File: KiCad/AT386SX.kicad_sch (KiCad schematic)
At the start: 33 parts, among them J10 OSC_PIN1, J11 OSC_PIN8, Q3 2N3904, U2 74HC05, U6 ICW42C07, U7 Cx486SLC, U8 80387SX, U9 RC2016A5, X2 14.31818MHz

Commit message: Version 1.5: Add filtering capacitors
Signed-off-by: Sergey Kiselev <skiselev@gmail.com>
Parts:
- R13: footprint My_Components:Res_Axial_L6.3mm_D2.5mm_P10.16mm_Horizontal -> My_Components:Res_762
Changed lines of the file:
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@@
       (effects (font (size 1.27 1.27)) (justify left))
     )
-    (property "Footprint" "My_Components:Res_Axial_L6.3mm_D2.5mm_P10.16mm_Horizontal" (id 2) (at 239.522 207.01 90)
+    (property "Footprint" "My_Components:Res_762" (id 2) (at 239.522 207.01 90)
       (effects (font (size 1.27 1.27)) hide)
     )
@@
   )
   (symbol_instances
+    (path "/b540f997-cabb-4061-85a0-370b4e9dd03a/c0e940d1-2426-4cbd-9a9b-134c5c650fe6"
+      (reference "#FLG01") (unit 1) (value "PWR_FLAG") (footprint "")
+    )
+    (path "/b540f997-cabb-4061-85a0-370b4e9dd03a/2758a6ac-f07f-4e7c-83ad-7d9a34e4f2bd"
+      (reference "#FLG02") (unit 1) (value "PWR_FLAG") (footprint "")
+    )
     (path "/1c0f074e-275c-4c09-93e3-0959df27fb02/9751a7f0-e700-4753-8324-be24a75a4a6c"
       (reference "#FLG0101") (unit 1) (value "PWR_FLAG") (footprint "")
@@
       (reference "#FLG0103") (unit 1) (value "PWR_FLAG") (footprint "")
     )
-    (path "/b540f997-cabb-4061-85a0-370b4e9dd03a/0338c4db-c33f-45e8-8989-5af966eadf04"
-      (reference "#FLG0104") (unit 1) (value "PWR_FLAG") (footprint "")
-    )
     (path "/b540f997-cabb-4061-85a0-370b4e9dd03a/e285e334-2dc0-407d-a384-e1491c80ffa6"
       (reference "#FLG0105") (unit 1) (value "PWR_FLAG") (footprint "")
     )
-    (path "/b540f997-cabb-4061-85a0-370b4e9dd03a/cdc8d8e2-b0ee-4c76-a0c0-bd7107912b4a"
-      (reference "#FLG0106") (unit 1) (value "PWR_FLAG") (footprint "")
-    )
     (path "/b540f997-cabb-4061-85a0-370b4e9dd03a/1a7d0fff-6458-426d-8397-de30782b2d34"
       (reference "#PWR0101") (unit 1) (value "GND") (footprint "")
@@
       (reference "#PWR0155") (unit 1) (value "VCC") (footprint "")
     )
+    (path "/b540f997-cabb-4061-85a0-370b4e9dd03a/53d85d0a-ae75-44bf-aff8-0d14c3b835b5"
+      (reference "#PWR0156") (unit 1) (value "VCC") (footprint "")
+    )
     (path "/b540f997-cabb-4061-85a0-370b4e9dd03a/f7b625b8-3877-4549-89fa-b234d7c48294"
       (reference "#PWR0157") (unit 1) (value "GND") (footprint "")
     )
-    (path "/b540f997-cabb-4061-85a0-370b4e9dd03a/846cd0cf-749b-4032-9d8a-86cf301d5632"
-      (reference "#PWR0158") (unit 1) (value "VCC") (footprint "")
-    )
     (path "/5f5198df-7309-40ea-b4e0-3ab5dbf9b838"
       (reference "#PWR0159") (unit 1) (value "GND") (footprint "")
@@
       (reference "#PWR0160") (unit 1) (value "GND") (footprint "")
     )
-    (path "/b540f997-cabb-4061-85a0-370b4e9dd03a/5351b270-0d2f-4dc2-b7a8-6ef3ae480c70"
-      (reference "#PWR0161") (unit 1) (value "VCC") (footprint "")
-    )
-    (path "/b540f997-cabb-4061-85a0-370b4e9dd03a/f7c64ee0-2580-4e51-a416-0697d5326aec"
-      (reference "#PWR0162") (unit 1) (value "VCC") (footprint "")
-    )
     (path "/b540f997-cabb-4061-85a0-370b4e9dd03a/0aa59643-6135-4806-bff4-0a5629df0518"
       (reference "#PWR0163") (unit 1) (value "VCC") (footprint "")
@@
       (reference "C1") (unit 1) (value "10uF") (footprint "My_Components:Cap_Elec_Radial_5mm_2.5mm")
     )
+    (path "/b540f997-cabb-4061-85a0-370b4e9dd03a/866f27b2-3b82-43ca-9630-39cc8b496338"
+      (reference "C2") (unit 1) (value "10uF") (footprint "My_Components:Cap_Elec_Radial_5mm_2.5mm")
+    )
+    (path "/b540f997-cabb-4061-85a0-370b4e9dd03a/acee4479-6f6d-41b4-b693-5e83c3878033"
+      (reference "C3") (unit 1) (value "10uF") (footprint "My_Components:Cap_Elec_Radial_5mm_2.5mm")
+    )
     (path "/b540f997-cabb-4061-85a0-370b4e9dd03a/00000000-0000-0000-0000-000063bb05ab"
       (reference "C4") (unit 1) (value "10uF") (footprint "My_Components:Cap_Elec_Radial_5mm_2.5mm")
@@
       (reference "C20") (unit 1) (value "100nF") (footprint "My_Components:Cap_Cer_508")
     )
-    (path "/b540f997-cabb-4061-85a0-370b4e9dd03a/82107f31-d66f-4484-b863-440418056f78"
-      (reference "C21") (unit 1) (value "100nF") (footprint "My_Components:Cap_Cer_508")
+    (path "/b540f997-cabb-4061-85a0-370b4e9dd03a/83e6d6e6-3a0e-4f35-9aac-5a1696ccc4a8"
+      (reference "C21") (unit 1) (value "10uF") (footprint "My_Components:Cap_Elec_Radial_5mm_2.5mm")
     )
     (path "/b540f997-cabb-4061-85a0-370b4e9dd03a/d300db72-0aab-4b42-b7a7-c0f30136b687"
       (reference "C22") (unit 1) (value "100nF") (footprint "My_Components:Cap_Cer_508")
     )
-    (path "/b540f997-cabb-4061-85a0-370b4e9dd03a/f9f9d52c-c3cf-4935-8d1b-0924649d81e5"
-      (reference "C24") (unit 1) (value "100nF") (footprint "My_Components:Cap_Cer_508")
-    )
-    (path "/b540f997-cabb-4061-85a0-370b4e9dd03a/e5a4a884-d89f-432e-8508-dc02115f736e"
-      (reference "C25") (unit 1) (value "100nF") (footprint "My_Components:Cap_Cer_508")
+    (path "/b540f997-cabb-4061-85a0-370b4e9dd03a/d44ce32e-e673-45da-90ee-6b6c41271040"
+      (reference "C24") (unit 1) (value "10uF") (footprint "My_Components:Cap_Elec_Radial_5mm_2.5mm")
+    )
+    (path "/b540f997-cabb-4061-85a0-370b4e9dd03a/58fee7c8-7975-4989-b550-51ecadfbd81a"
+      (reference "C25") (unit 1) (value "10uF") (footprint "My_Components:Cap_Elec_Radial_5mm_2.5mm")
+    )
+    (path "/b540f997-cabb-4061-85a0-370b4e9dd03a/72c93df4-901b-461c-920a-5af57e8f3b34"
+      (reference "C26") (unit 1) (value "10uF") (footprint "My_Components:Cap_Elec_Radial_5mm_2.5mm")
+    )
+    (path "/b540f997-cabb-4061-85a0-370b4e9dd03a/a403b7ba-4f6e-4ddc-9b0d-0272dd53c8b1"
+      (reference "C27") (unit 1) (value "10uF") (footprint "My_Components:Cap_Elec_Radial_5mm_2.5mm")
     )
     (path "/b540f997-cabb-4061-85a0-370b4e9dd03a/00000000-0000-0000-0000-000063bb0fa8"
@@
       (reference "C29") (unit 1) (value "10uF") (footprint "My_Components:Cap_Elec_Radial_5mm_2.5mm")
     )
+    (path "/b540f997-cabb-4061-85a0-370b4e9dd03a/16473865-3bb2-4dc5-b29e-12be28744a4c"
+      (reference "C30") (unit 1) (value "10uF") (footprint "My_Components:Cap_Elec_Radial_5mm_2.5mm")
+    )
+    (path "/b540f997-cabb-4061-85a0-370b4e9dd03a/43bba2de-b2e8-44ad-b2d4-e209d0f942ad"
+      (reference "C31") (unit 1) (value "10uF") (footprint "My_Components:Cap_Elec_Radial_5mm_2.5mm")
+    )
     (path "/b540f997-cabb-4061-85a0-370b4e9dd03a/d232d0eb-3f13-4834-9c33-70f4e6a8a01d"
       (reference "C32") (unit 1) (value "100nF") (footprint "My_Components:Cap_Cer_508")
@@
       (reference "C34") (unit 1) (value "10uF") (footprint "My_Components:Cap_Elec_Radial_5mm_2.5mm")
     )
+    (path "/b540f997-cabb-4061-85a0-370b4e9dd03a/3110a922-14a0-44ef-a54c-3b575cbe8b26"
+      (reference "C35") (unit 1) (value "10uF") (footprint "My_Components:Cap_Elec_Radial_5mm_2.5mm")
+    )
     (path "/b26fa998-147e-4a4a-acf7-0978c0b5329c"
       (reference "C36") (unit 1) (value "30pF") (footprint "My_Components:Cap_Cer_508")
@@
       (reference "C50") (unit 1) (value "100nF") (footprint "My_Components:Cap_Cer_508")
     )
-    (path "/b540f997-cabb-4061-85a0-370b4e9dd03a/6584f64a-9ab4-4f31-82b0-75bb3fe070ee"
-      (reference "C51") (unit 1) (value "C") (footprint "My_Components:Cap_Cer_508")
-    )
     (path "/b540f997-cabb-4061-85a0-370b4e9dd03a/4287aab0-4184-45db-a75d-09310ed89582"
       (reference "C52") (unit 1) (value "C") (footprint "My_Components:Cap_Cer_508")
     )
-    (path "/b540f997-cabb-4061-85a0-370b4e9dd03a/1f08831b-e9f5-446b-ba9c-03d3cf6d80fa"
-      (reference "C53") (unit 1) (value "C") (footprint "My_Components:Cap_Cer_508")
-    )
     (path "/b540f997-cabb-4061-85a0-370b4e9dd03a/70df511f-ea42-424c-a171-ecadeb0a7b2e"
       (reference "C54") (unit 1) (value "C") (footprint "My_Components:Cap_Cer_508")
@@
     )
     (path "/dfd81590-8c6f-413e-ae3f-c6cd719d418a"
-      (reference "R13") (unit 1) (value "330") (footprint "My_Components:Res_Axial_L6.3mm_D2.5mm_P10.16mm_Horizontal")
-    )
-    (path "/b540f997-cabb-4061-85a0-370b4e9dd03a/78faf1cf-3103-45dc-9c03-6ae58af91042"
-      (reference "R14") (unit 1) (value "4.7k") (footprint "My_Components:Res_Axial_L6.3mm_D2.5mm_P10.16mm_Horizontal")
-    )
-    (path "/b540f997-cabb-4061-85a0-370b4e9dd03a/922bd17d-5d03-410d-a371-736377126c8b"
-      (reference "R15") (unit 1) (value "4.7k") (footprint "My_Components:Res_Axial_L6.3mm_D2.5mm_P10.16mm_Horizontal")
-    )
-    (path "/b540f997-cabb-4061-85a0-370b4e9dd03a/a706534b-46c9-4794-82e7-eca4df7992f0"
-      (reference "R16") (unit 1) (value "4.7k") (footprint "My_Components:Res_Axial_L6.3mm_D2.5mm_P10.16mm_Horizontal")
+      (reference "R13") (unit 1) (value "330") (footprint "My_Components:Res_762")
     )
     (path "/1c0f074e-275c-4c09-93e3-0959df27fb02/8ada6564-4809-42ed-8975-d5ba2059e9ee"
@@
     )
     (path "/b540f997-cabb-4061-85a0-370b4e9dd03a/93c871f6-7228-4841-9ed4-d13359d0f749"
-      (reference "R31") (unit 1) (value "1k") (footprint "My_Components:Res_Axial_L6.3mm_D2.5mm_P10.16mm_Horizontal")
+      (reference "R31") (unit 1) (value "1k") (footprint "My_Components:Res_762")
     )
     (path "/56ab2f9d-f360-4763-a520-1236cf082aa2"
       (reference "R32") (unit 1) (value "DNP") (footprint "My_Components:Res_Axial_L6.3mm_D2.5mm_P10.16mm_Horizontal")
     )
+    (path "/b540f997-cabb-4061-85a0-370b4e9dd03a/f685576f-2d5f-436b-8674-c8934ee81303"
+      (reference "RN9") (unit 1) (value "4.7k") (footprint "My_Components:Conn_SIL6")
+    )
     (path "/b540f997-cabb-4061-85a0-370b4e9dd03a/15c5cb70-9076-4d0d-8d62-4d5b5f0b4f83"
       (reference "RP1") (unit 1) (value "4.7k") (footprint "My_Components:Conn_SIL9")
     )
-    (path "/b540f997-cabb-4061-85a0-370b4e9dd03a/bab055f8-1a41-477e-976a-dc247909eaa3"
-      (reference "RP2") (unit 1) (value "4.7k") (footprint "My_Components:Conn_SIL9")
+    (path "/b540f997-cabb-4061-85a0-370b4e9dd03a/47821b7e-104b-48e6-86f2-072c2a1b5313"
+      (reference "RP2") (unit 1) (value "4.7k") (footprint "My_Components:Conn_SIL6")
     )
     (path "/b540f997-cabb-4061-85a0-370b4e9dd03a/483c61d0-cbab-49b2-9bde-e0b4ad354ffa"

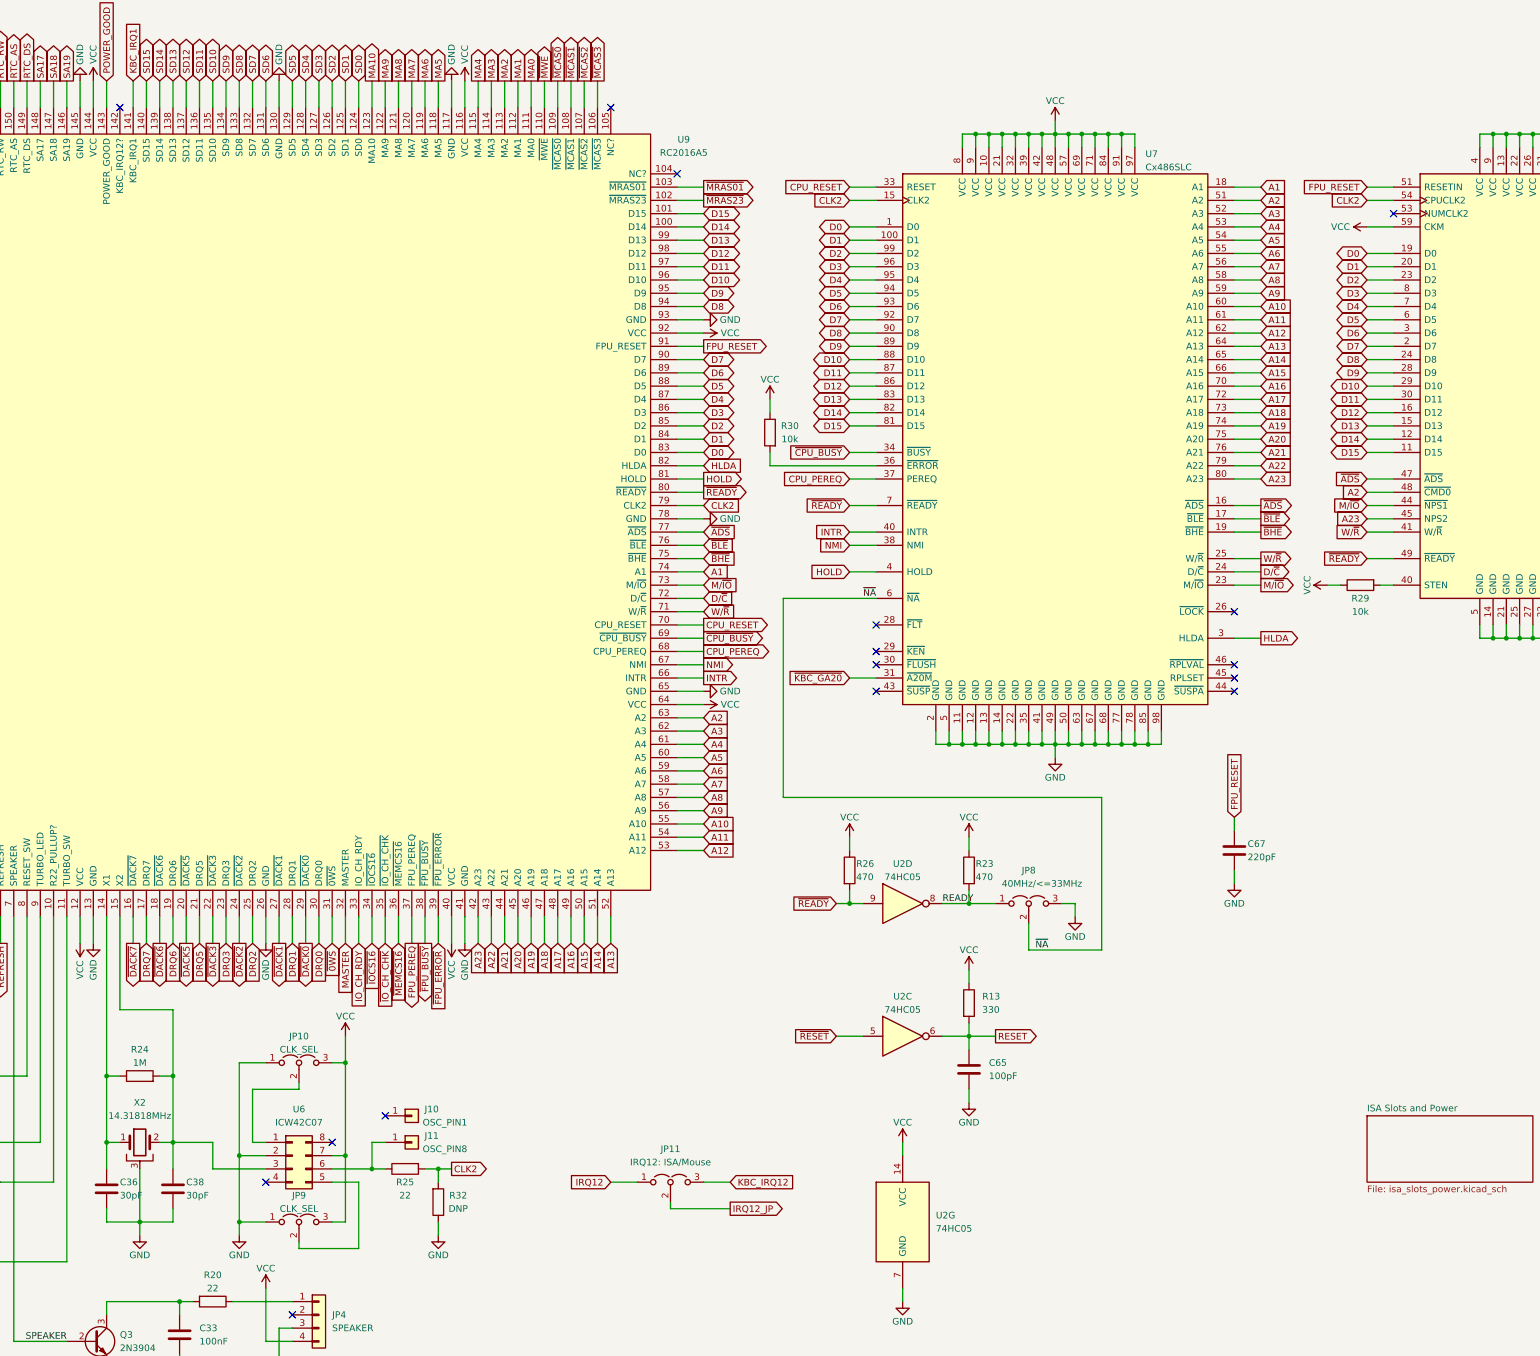
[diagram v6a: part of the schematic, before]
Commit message: Version 1.6: Use half-can oscillators and low-profile crystal
Signed-off-by: Sergey Kiselev <skiselev@gmail.com>
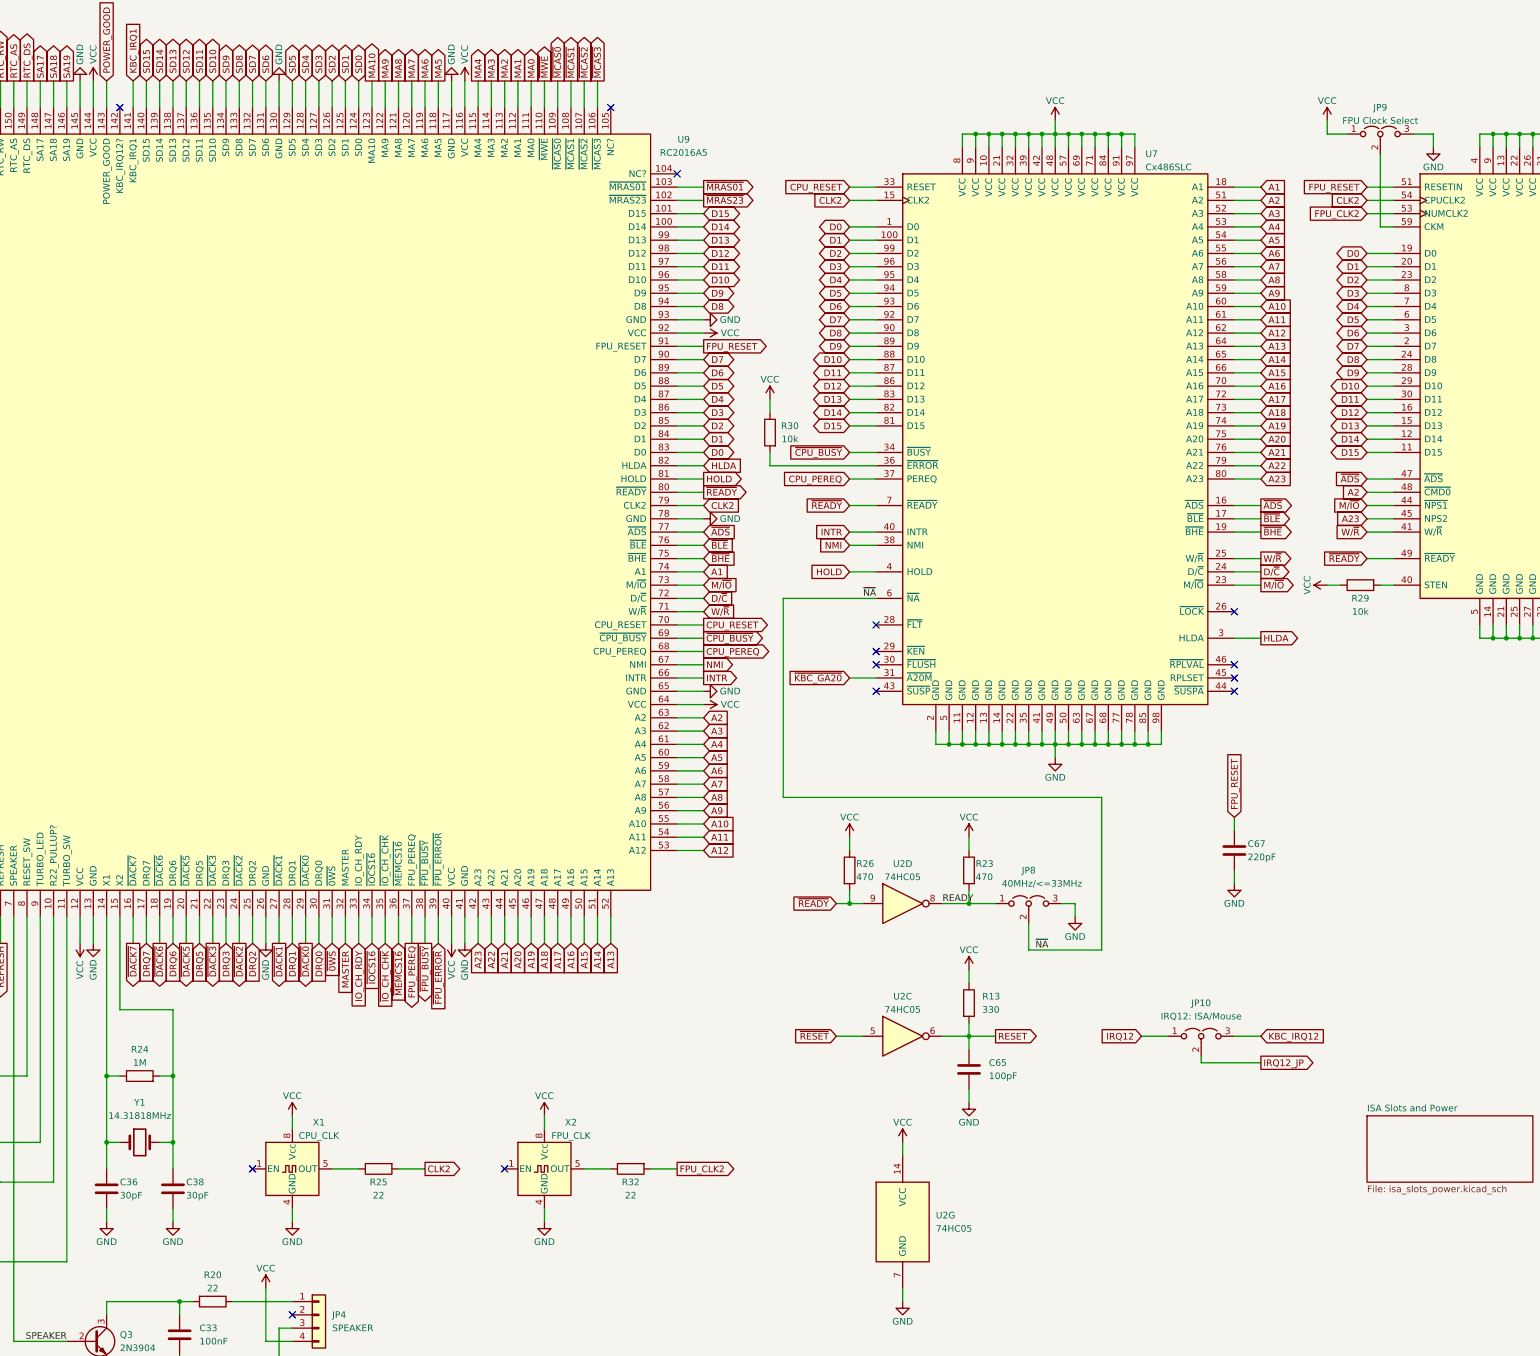
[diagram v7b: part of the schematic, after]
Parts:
- removed J10: OSC_PIN1, My_Components:Conn_Pin_Header_1x1_2.54mm_NoKey, symbol Connector_Generic:Conn_01x01
- removed J11: OSC_PIN8, My_Components:Conn_Pin_Header_1x1_2.54mm_NoKey, symbol Connector_Generic:Conn_01x01
- removed JP10: CLK_SEL, My_Components:Conn_Pin_Header_3x1_2.54mm, symbol Jumper:Jumper_3_Open
- removed U6: ICW42C07, My_Components:IC_DIP8_300, symbol Connector_Generic:Conn_02x04_Counter_Clockwise
- removed X2: 14.31818MHz, My_Components:Crystal_HC-49U_Horiz, symbol Device:Crystal_GND3
- added X1: CPU_CLK, My_Components:OSC_Half_Can_DIP8, symbol Oscillator:CXO_DIP8
- added X2: FPU_CLK, My_Components:OSC_Half_Can_DIP8, symbol Oscillator:CXO_DIP8
- added Y1: 14.31818MHz, My_Components:Crystal_HC-49U_Vert, symbol Device:Crystal
- JP9: value CLK_SEL -> FPU Clock Select
- R20, R22, R23, R24, R25, R26, R28, R29, R30: footprint My_Components:Res_Axial_L6.3mm_D2.5mm_P10.16mm_Horizontal -> My_Components:Res_762
- R32: value DNP -> 22; footprint My_Components:Res_Axial_L6.3mm_D2.5mm_P10.16mm_Horizontal -> My_Components:Res_762
- renumbered JP11 to JP10
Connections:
- net CLK2: no longer R32.2
- net GND: now also JP9.3 (B), X1.4 (GND), X2.4 (GND); no longer JP9.1 (A), R32.1
- net VCC: now also JP9.1 (A), X1.8 (Vcc), X2.8 (Vcc); no longer JP9.3 (B), U8.59 (CKM)
- net at C38.1, R24.2, U9.15 (X2): now also Y1.2
- net at JP9.2 (C): now also U8.59 (CKM)
- net at R25.1: now also X1.5 (OUT)
- net at C36.1, R24.1, U9.14 (X1): now also Y1.1
- net FPU_CLK2: now reaches U8.53 (NUMCLK2)
- net FPU_CLK2: now also R32.2
- new net: R32.1, X2.5 (OUT)
- no-connect marks 18 -> 16
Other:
- moved on the sheet: JP10, JP9, R25
